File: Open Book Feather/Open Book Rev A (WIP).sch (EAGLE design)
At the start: 111 parts, among them J1 SJ-43514-SMT, J2 10118193-0001LF, Q1 DMG341, Q2 IRLML0100, SW1 SPDT_SWITCH, U1 AP2112-3.3, U2 MCP73831T-2ACI/OT, U3 ATSAMD51J64-TQFP(10X10), U4 GD25Q64, U5 74AC165D, U7 23K256-I/SN, X1 JSTPH, X2 2x5 0.05" SWD

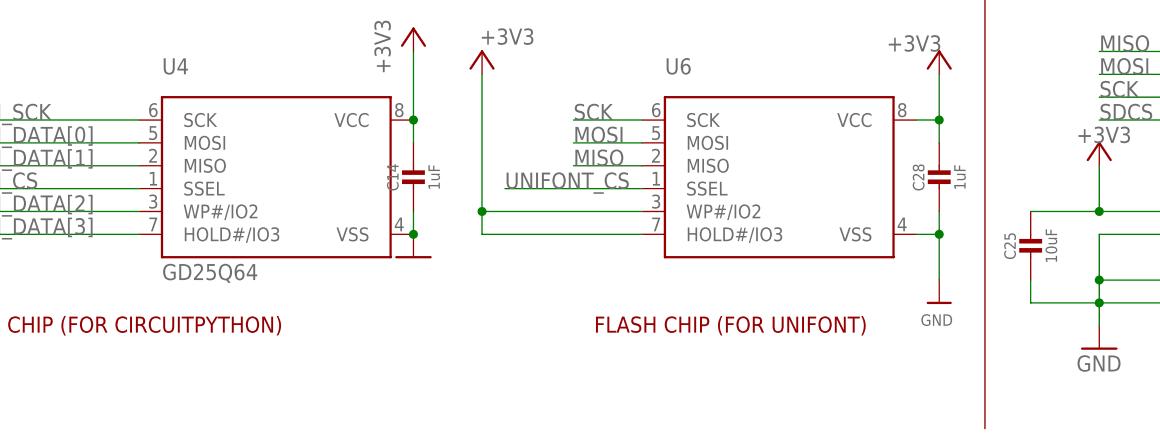
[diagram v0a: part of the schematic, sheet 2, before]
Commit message: clarify flash chips
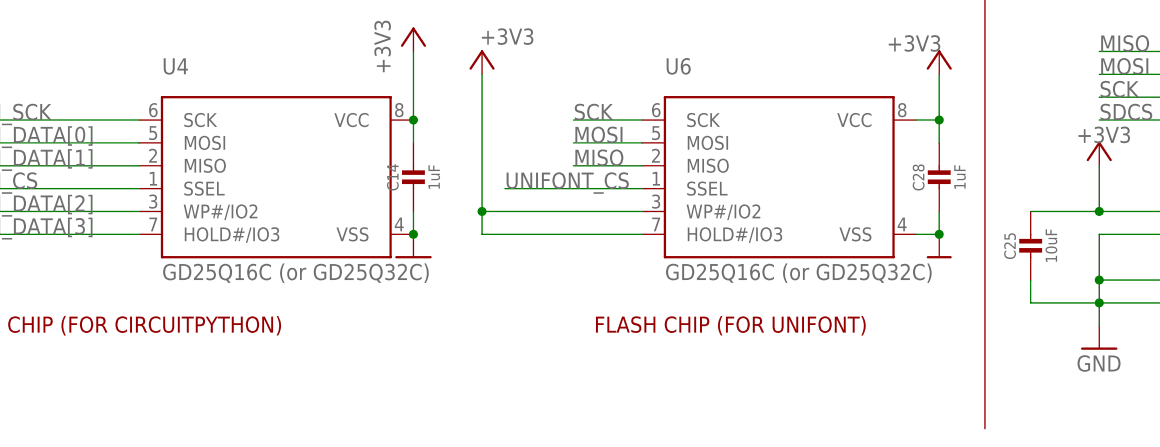
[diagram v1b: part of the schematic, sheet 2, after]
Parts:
- U4: value GD25Q64 -> GD25Q16C (or GD25Q32C)
- U6: value (none) -> GD25Q16C (or GD25Q32C)
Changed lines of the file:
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@@
 <part name="R14" library="microbuilder" deviceset="RESISTOR" device="0805_NOOUTLINE" value="100K"/>
 <part name="R2" library="microbuilder" deviceset="RESISTOR" device="0805_NOOUTLINE" value="100K"/>
-<part name="U4" library="microbuilder" deviceset="SPIFLASH_8PIN" device="" value="GD25Q64"/>
+<part name="U4" library="microbuilder" deviceset="SPIFLASH_8PIN" device="" value="GD25Q16C (or GD25Q32C)"/>
 <part name="GND25" library="supply1" deviceset="GND" device=""/>
 <part name="+3V28" library="supply1" deviceset="+3V3" device=""/>
@@
 <part name="U$41" library="microbuilder" deviceset="GND" device=""/>
 <part name="U$23" library="My Stuff" deviceset="OSO-TEXT-TEST" device=""/>
-<part name="U6" library="Adafruit Feather M0 Express" deviceset="MICROBUILDER_SPIFLASH_SOIC8" device=""/>
+<part name="U6" library="Adafruit Feather M0 Express" deviceset="MICROBUILDER_SPIFLASH_SOIC8" device="" value="GD25Q16C (or GD25Q32C)"/>
 <part name="+3V15" library="supply1" library_urn="urn:adsk.eagle:library:371" deviceset="+3V3" device=""/>
 <part name="+3V16" library="supply1" library_urn="urn:adsk.eagle:library:371" deviceset="+3V3" device=""/>
@@
 <attribute name="VALUE" x="116.078" y="45.72" size="1.778" layer="96"/>
 </instance>
-<instance part="U$40" gate="G$1" x="121.92" y="17.78" smashed="yes" rot="MR0">
-<attribute name="VALUE" x="123.444" y="15.24" size="1.27" layer="96" rot="MR0"/>
-</instance>
+<instance part="U$40" gate="G$1" x="121.92" y="22.86" smashed="yes" rot="MR0"/>
 <instance part="C28" gate="G$1" x="121.92" y="30.48" smashed="yes">
 <attribute name="NAME" x="119.63" y="31.73" size="1.27" layer="95" font="vector" rot="R90" align="center"/>
@@
 <wire x1="121.92" y1="25.4" x2="121.92" y2="27.94" width="0.1524" layer="91"/>
 <pinref part="U$40" gate="G$1" pin="GND"/>
-<wire x1="121.92" y1="25.4" x2="121.92" y2="20.32" width="0.1524" layer="91"/>
 <junction x="121.92" y="25.4"/>
 </segment>

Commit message: add logos and such
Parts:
- added U$44: OSO_GRAPHIC, My Stuff:OSO_GRAPHIC
- added U$45: OSO_BEAR, My Stuff:OSO_BEAR
- added U$47: OSO_TEXT, My Stuff:OSO_TEXT
- added U$48: OSO_TEXTOSO_TEXT_ONELINE_125MIL, My Stuff:OSO_TEXTOSO_TEXT_ONELINE_125MIL
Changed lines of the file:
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@@
 <?xml version="1.0" encoding="utf-8"?>
 <!DOCTYPE eagle SYSTEM "eagle.dtd">
-<eagle version="9.4.2">
+<eagle version="9.3.0">
 <drawing>
 <settings>
@@
 <part name="GND7" library="supply1" deviceset="GND" device=""/>
 <part name="C8" library="microbuilder" deviceset="CAP_CERAMIC" device="0805_10MGAP" value="1uF"/>
+<part name="U$44" library="My Stuff" deviceset="OSO_GRAPHIC" device=""/>
+<part name="U$45" library="My Stuff" deviceset="OSO_BEAR" device=""/>
+<part name="U$47" library="My Stuff" deviceset="OSO_TEXT" device=""/>
+<part name="U$48" library="My Stuff" deviceset="OSO_TEXT" device="OSO_TEXT_ONELINE_125MIL"/>
 </parts>
 <sheets>
@@
 <attribute name="VALUE" x="169.926" y="170.942" size="1.778" layer="96"/>
 </instance>
+<instance part="U$44" gate="G$1" x="264.16" y="63.5" smashed="yes"/>
+<instance part="U$45" gate="G$1" x="312.42" y="73.66" smashed="yes"/>
+<instance part="U$47" gate="G$1" x="297.18" y="50.8" smashed="yes"/>
+<instance part="U$48" gate="G$1" x="309.88" y="58.42" smashed="yes"/>
 </instances>
 <busses>

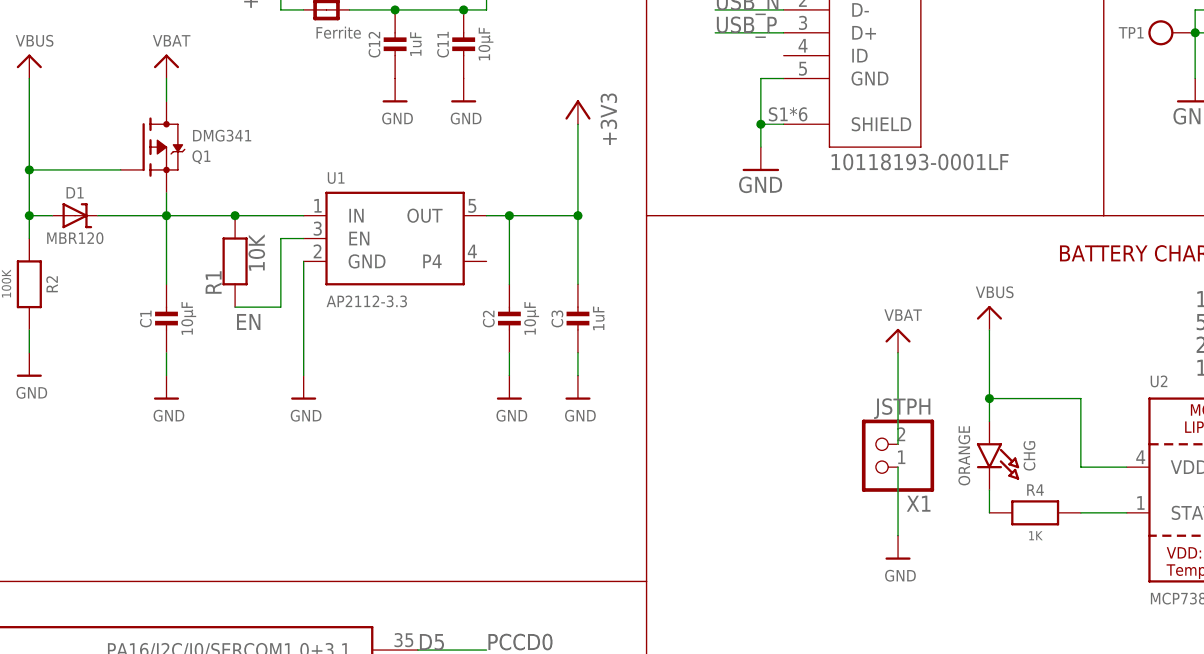
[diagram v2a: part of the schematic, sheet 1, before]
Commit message: move leds topside, thru-hole style. other design tweaks
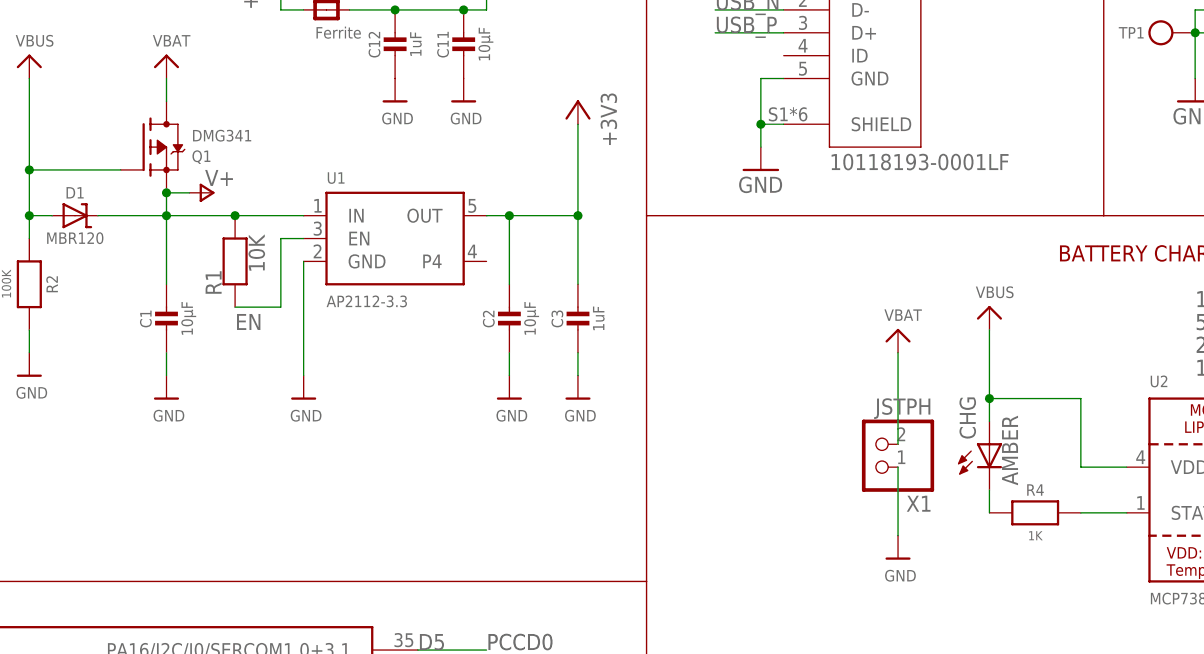
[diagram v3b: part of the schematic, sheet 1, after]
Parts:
- removed LED1: WS2812B3535, microbuilder:WS2812B3535
- added STATUS: WS2812B, adafruit:WS2812B
- CHG: value ORANGE -> AMBER; device microbuilder:LED0805_NOOUTLINE -> adafruit:LED3MM
- LED: value RED -> RED OR GRN; device microbuilder:LED0805_NOOUTLINE -> adafruit:LED3MM
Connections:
- removed net VHI: C1.1, D1.C, Q1.S, R1.2, U1.IN
- new net V+: C1.1, D1.C, Q1.S, R1.2, STATUS.VDD, U1.IN
- net +3V3: no longer LED1.VDD
- net D8_NEOPIX: now also STATUS.DI; no longer LED1.DI
- net GND: now also STATUS.GND; no longer LED1.GND

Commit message: add these cool right-angle LEDs (that i ordered too many of)
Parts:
- CHG, LED: device adafruit:LED3MM -> adafruit:LEDVISHAY_SIDEVIEW
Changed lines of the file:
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@@
 <grid distance="0.1" unitdist="inch" unit="inch" style="lines" multiple="1" display="no" altdistance="0.01" altunitdist="inch" altunit="inch"/>
 <layers>
-<layer number="1" name="Top" color="4" fill="1" visible="no" active="no"/>
-<layer number="2" name="Route2" color="1" fill="3" visible="no" active="no"/>
-<layer number="3" name="Route3" color="4" fill="3" visible="no" active="no"/>
-<layer number="4" name="Route4" color="1" fill="4" visible="no" active="no"/>
-<layer number="5" name="Route5" color="4" fill="4" visible="no" active="no"/>
-<layer number="6" name="Route6" color="1" fill="8" visible="no" active="no"/>
-<layer number="7" name="Route7" color="4" fill="8" visible="no" active="no"/>
-<layer number="8" name="Route8" color="1" fill="2" visible="no" active="no"/>
-<layer number="9" name="Route9" color="4" fill="2" visible="no" active="no"/>
-<layer number="10" name="Route10" color="1" fill="7" visible="no" active="no"/>
-<layer number="11" name="Route11" color="4" fill="7" visible="no" active="no"/>
-<layer number="12" name="Route12" color="1" fill="5" visible="no" active="no"/>
-<layer number="13" name="Route13" color="4" fill="5" visible="no" active="no"/>
-<layer number="14" name="Route14" color="1" fill="6" visible="no" active="no"/>
-<layer number="15" name="Route15" color="4" fill="6" visible="no" active="no"/>
-<layer number="16" name="Bottom" color="1" fill="1" visible="no" active="no"/>
-<layer number="17" name="Pads" color="2" fill="1" visible="no" active="no"/>
-<layer number="18" name="Vias" color="2" fill="1" visible="no" active="no"/>
-<layer number="19" name="Unrouted" color="6" fill="1" visible="no" active="no"/>
-<layer number="20" name="Dimension" color="15" fill="1" visible="no" active="no"/>
-<layer number="21" name="tPlace" color="14" fill="1" visible="no" active="no"/>
-<layer number="22" name="bPlace" color="13" fill="1" visible="no" active="no"/>
-<layer number="23" name="tOrigins" color="15" fill="1" visible="no" active="no"/>
-<layer number="24" name="bOrigins" color="15" fill="1" visible="no" active="no"/>
-<layer number="25" name="tNames" color="7" fill="1" visible="no" active="no"/>
-<layer number="26" name="bNames" color="7" fill="1" visible="no" active="no"/>
-<layer number="27" name="tValues" color="7" fill="1" visible="no" active="no"/>
-<layer number="28" name="bValues" color="7" fill="1" visible="no" active="no"/>
+<layer number="1" name="Top" color="4" fill="1" visible="yes" active="no"/>
+<layer number="2" name="Route2" color="1" fill="3" visible="yes" active="no"/>
+<layer number="3" name="Route3" color="4" fill="3" visible="yes" active="no"/>
+<layer number="4" name="Route4" color="1" fill="4" visible="yes" active="no"/>
+<layer number="5" name="Route5" color="4" fill="4" visible="yes" active="no"/>
+<layer number="6" name="Route6" color="1" fill="8" visible="yes" active="no"/>
+<layer number="7" name="Route7" color="4" fill="8" visible="yes" active="no"/>
+<layer number="8" name="Route8" color="1" fill="2" visible="yes" active="no"/>
+<layer number="9" name="Route9" color="4" fill="2" visible="yes" active="no"/>
+<layer number="10" name="Route10" color="1" fill="7" visible="yes" active="no"/>
+<layer number="11" name="Route11" color="4" fill="7" visible="yes" active="no"/>
+<layer number="12" name="Route12" color="1" fill="5" visible="yes" active="no"/>
+<layer number="13" name="Route13" color="4" fill="5" visible="yes" active="no"/>
+<layer number="14" name="Route14" color="1" fill="6" visible="yes" active="no"/>
+<layer number="15" name="Route15" color="4" fill="6" visible="yes" active="no"/>
+<layer number="16" name="Bottom" color="1" fill="1" visible="yes" active="no"/>
+<layer number="17" name="Pads" color="2" fill="1" visible="yes" active="no"/>
+<layer number="18" name="Vias" color="2" fill="1" visible="yes" active="no"/>
+<layer number="19" name="Unrouted" color="6" fill="1" visible="yes" active="no"/>
+<layer number="20" name="Dimension" color="15" fill="1" visible="yes" active="no"/>
+<layer number="21" name="tPlace" color="14" fill="1" visible="yes" active="no"/>
+<layer number="22" name="bPlace" color="13" fill="1" visible="yes" active="no"/>
+<layer number="23" name="tOrigins" color="15" fill="1" visible="yes" active="no"/>
+<layer number="24" name="bOrigins" color="15" fill="1" visible="yes" active="no"/>
+<layer number="25" name="tNames" color="7" fill="1" visible="yes" active="no"/>
+<layer number="26" name="bNames" color="7" fill="1" visible="yes" active="no"/>
+<layer number="27" name="tValues" color="7" fill="1" visible="yes" active="no"/>
+<layer number="28" name="bValues" color="7" fill="1" visible="yes" active="no"/>
 <layer number="29" name="tStop" color="7" fill="3" visible="no" active="no"/>
 <layer number="30" name="bStop" color="7" fill="6" visible="no" active="no"/>
@@
 <layer number="35" name="tGlue" color="7" fill="4" visible="no" active="no"/>
 <layer number="36" name="bGlue" color="7" fill="5" visible="no" active="no"/>
-<layer number="37" name="tTest" color="7" fill="1" visible="no" active="no"/>
-<layer number="38" name="bTest" color="7" fill="1" visible="no" active="no"/>
+<layer number="37" name="tTest" color="7" fill="1" visible="yes" active="no"/>
+<layer number="38" name="bTest" color="7" fill="1" visible="yes" active="no"/>
 <layer number="39" name="tKeepout" color="4" fill="11" visible="no" active="no"/>
 <layer number="40" name="bKeepout" color="1" fill="11" visible="no" active="no"/>
@@
 <layer number="44" name="Drills" color="7" fill="1" visible="no" active="no"/>
 <layer number="45" name="Holes" color="7" fill="1" visible="no" active="no"/>
-<layer number="46" name="Milling" color="3" fill="1" visible="no" active="no"/>
-<layer number="47" name="Measures" color="7" fill="1" visible="no" active="no"/>
-<layer number="48" name="Document" color="7" fill="1" visible="no" active="no"/>
-<layer number="49" name="Reference" color="7" fill="1" visible="no" active="no"/>
-<layer number="50" name="dxf" color="7" fill="1" visible="no" active="no"/>
-<layer number="51" name="tDocu" color="7" fill="1" visible="no" active="no"/>
-<layer number="52" name="bDocu" color="7" fill="1" visible="no" active="no"/>
-<layer number="53" name="tGND_GNDA" color="7" fill="9" visible="no" active="no"/>
-<layer number="54" name="bGND_GNDA" color="1" fill="9" visible="no" active="no"/>
-<layer number="56" name="wert" color="7" fill="1" visible="no" active="no"/>
-<layer number="57" name="tCAD" color="7" fill="1" visible="no" active="no"/>
-<layer number="59" name="tCarbon" color="7" fill="1" visible="no" active="no"/>
-<layer number="60" name="bCarbon" color="7" fill="1" visible="no" active="no"/>
+<layer number="46" name="Milling" color="3" fill="1" visible="yes" active="no"/>
+<layer number="47" name="Measures" color="7" fill="1" visible="yes" active="no"/>
+<layer number="48" name="Document" color="7" fill="1" visible="yes" active="no"/>
+<layer number="49" name="Reference" color="7" fill="1" visible="yes" active="no"/>
+<layer number="50" name="dxf" color="7" fill="1" visible="yes" active="no"/>
+<layer number="51" name="tDocu" color="7" fill="1" visible="yes" active="no"/>
+<layer number="52" name="bDocu" color="7" fill="1" visible="yes" active="no"/>
+<layer number="53" name="tGND_GNDA" color="7" fill="9" visible="yes" active="no"/>
+<layer number="54" name="bGND_GNDA" color="1" fill="9" visible="yes" active="no"/>
+<layer number="56" name="wert" color="7" fill="1" visible="yes" active="no"/>
+<layer number="57" name="tCAD" color="7" fill="1" visible="yes" active="no"/>
+<layer number="59" name="tCarbon" color="7" fill="1" visible="yes" active="no"/>
+<layer number="60" name="bCarbon" color="7" fill="1" visible="yes" active="no"/>
 <layer number="88" name="SimResults" color="9" fill="1" visible="yes" active="yes"/>
 <layer number="89" name="SimProbes" color="9" fill="1" visible="yes" active="yes"/>
@@
 <part name="U$47" library="My Stuff" deviceset="OSO_TEXT" device=""/>
 <part name="U$48" library="My Stuff" deviceset="OSO_TEXT" device="OSO_TEXT_ONELINE_125MIL"/>
-<part name="LED" library="adafruit" deviceset="LED" device="3MM" value="RED OR GRN"/>
-<part name="CHG" library="adafruit" deviceset="LED" device="3MM" value="AMBER"/>
+<part name="LED" library="adafruit" deviceset="LED" device="VISHAY_SIDEVIEW" value="RED OR GRN"/>
+<part name="CHG" library="adafruit" deviceset="LED" device="VISHAY_SIDEVIEW" value="AMBER"/>
 <part name="STATUS" library="adafruit" deviceset="WS2812B" device=""/>
 <part name="P+1" library="supply1" library_urn="urn:adsk.eagle:library:371" deviceset="V+" device=""/>

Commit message: last minute tweaks to text and arrangement
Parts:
- removed MS2: FEATHERWING_SMTDUAL, microbuilder:FEATHERWING_SMTDUAL
- removed U$23: OSO-TEXT-TEST, My Stuff:OSO-TEXT-TEST
- added MS1: FEATHERWING_SMTDUAL, pygamer-microbuilder:FEATHERWING_SMTDUAL
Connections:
- net !RESET: now also MS1.!RESET; no longer MS2.!RESET
- net +3V3: now also MS1.3V; no longer MS2.3V
- net A0: now also MS1.GPIOA0; no longer MS2.GPIOA0
- net A1: now also MS1.GPIOA1; no longer MS2.GPIOA1
- net A2: now also MS1.GPIOA2; no longer MS2.GPIOA2
- net A3: now also MS1.GPIOA3; no longer MS2.GPIOA3
- net A4: now also MS1.GPIOA4; no longer MS2.GPIOA4
- net A5: now also MS1.GPIOA5; no longer MS2.GPIOA5
- net AVCC: now also MS1.AREF; no longer MS2.AREF
- net D10: now also MS1.GPIO10; no longer MS2.GPIO10
- net D11: now also MS1.GPIO11; no longer MS2.GPIO11
- net D12: now also MS1.GPIO12; no longer MS2.GPIO12
- net D13: now also MS1.GPIO13; no longer MS2.GPIO13
- net D5: now also MS1.GPIO5; no longer MS2.GPIO5
- net D6: now also MS1.GPIO6; no longer MS2.GPIO6
- net D9: now also MS1.GPIO9; no longer MS2.GPIO9
- net EN: now also MS1.EN; no longer MS2.EN
- net GND: now also MS1.GND, MS1.NC; no longer MS2.GND, MS2.NC
- net MISO: now also MS1.GPIOMISO; no longer MS2.GPIOMISO
- net MOSI: now also MS1.GPIOMOSI; no longer MS2.GPIOMOSI
- net RX: now also MS1.GPIORX; no longer MS2.GPIORX
- net SCK: now also MS1.GPIOSCK; no longer MS2.GPIOSCK
- net SCL: now also MS1.GPIOSCL; no longer MS2.GPIOSCL
- net SDA: now also MS1.GPIOSDA; no longer MS2.GPIOSDA
- net TX: now also MS1.GPIOTX; no longer MS2.GPIOTX
- net VBAT: now also MS1.VBAT; no longer MS2.VBAT
- net VBUS: now also MS1.USB; no longer MS2.USB
